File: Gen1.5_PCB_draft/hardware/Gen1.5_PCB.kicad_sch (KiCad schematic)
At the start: 35 parts, among them IC1 TJA1050T, J1 Enc1, J10 L3, J11 L4, J12 Enc2, J13 Enc3, J14 Enc4, J2 IMU, J3 Booster, J4 CAN, J5 Roboclaw1, J6 Roboclaw2, J7 Roboclaw3, J8 L1, J9 L2, U1 ESP32-P4-ETH, U2 level shifter

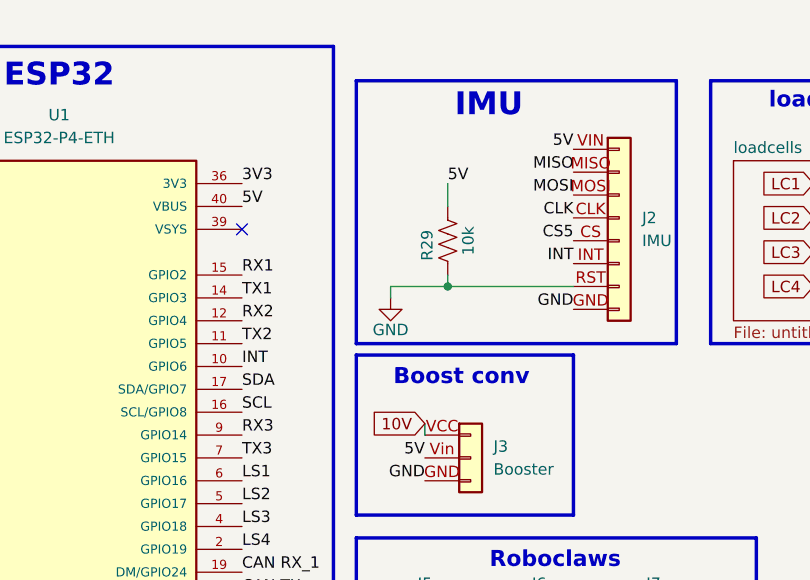
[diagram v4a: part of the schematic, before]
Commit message: fixed can test circuit via sizing
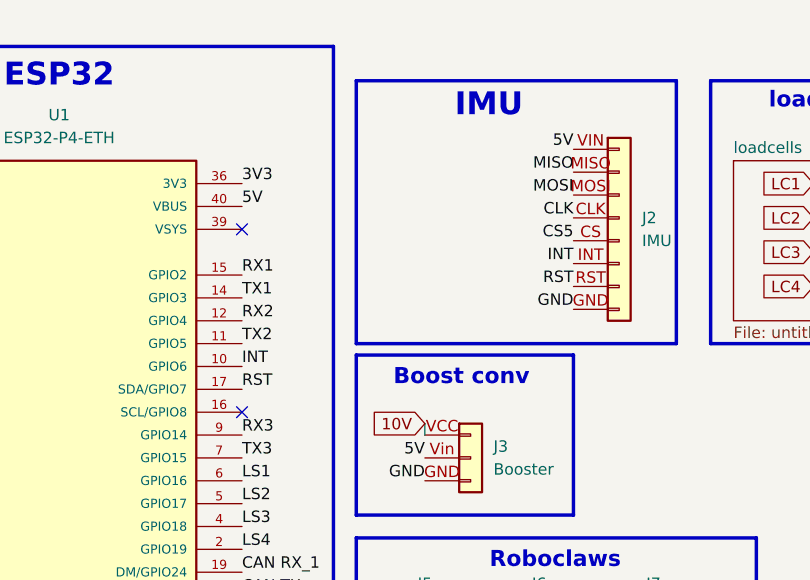
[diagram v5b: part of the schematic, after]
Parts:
- removed R29: 10k, symbol Device:R_US
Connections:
- net GND: no longer J2.RST (Pin_7)
- net SCL: no longer names the net of U1.16 (SCL/GPIO8)
- net SDA renamed RST
- net RST: now also J2.RST (Pin_7)
- no-connect marks 4 -> 5
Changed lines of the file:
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@@
 	)
 	(junction
-		(at 90.17 139.7)
-		(diameter 0)
-		(color 0 0 0 0)
-	)
-	(junction
 		(at 234.95 43.18)
 		(diameter 0)
@@
 	)
 	(no_connect
+		(at 67.31 153.67)
+	)
+	(no_connect
 		(at 26.67 138.43)
 	)
@@
 	(wire
 		(pts
-			(xy 104.14 139.7) (xy 90.17 139.7)
-		)
-		(stroke
-			(width 0)
-			(type default)
-		)
-	)
-	(wire
-		(pts
 			(xy 219.71 64.77) (xy 234.95 64.77)
 		)
@@
 	(wire
 		(pts
-			(xy 83.82 139.7) (xy 83.82 140.97)
-		)
-		(stroke
-			(width 0)
-			(type default)
-		)
-	)
-	(wire
-		(pts
 			(xy 93.98 184.15) (xy 93.98 185.42)
 		)
@@
 	(wire
 		(pts
-			(xy 90.17 139.7) (xy 83.82 139.7)
-		)
-		(stroke
-			(width 0)
-			(type default)
-		)
-	)
-	(wire
-		(pts
-			(xy 90.17 128.27) (xy 90.17 130.81)
-		)
-		(stroke
-			(width 0)
-			(type default)
-		)
-	)
-	(wire
-		(pts
 			(xy 175.26 119.38) (xy 186.69 119.38)
 		)
@@
 	(wire
 		(pts
-			(xy 90.17 138.43) (xy 90.17 139.7)
-		)
-		(stroke
-			(width 0)
-			(type default)
-		)
-	)
-	(wire
-		(pts
 			(xy 97.79 92.71) (xy 97.79 96.52)
 		)
@@
 		)
 	)
+	(label "RST"
+		(at 67.31 151.13 0)
+		(effects
+			(font
+				(size 1.27 1.27)
+			)
+			(justify left bottom)
+		)
+	)
 	(label "3V3"
 		(at 45.72 85.09 180)
@@
 		)
 	)
-	(label "SDA"
-		(at 67.31 151.13 0)
-		(effects
-			(font
-				(size 1.27 1.27)
-			)
-			(justify left bottom)
-		)
-	)
 	(label "MOSI"
 		(at 26.67 161.29 180)
@@
 		)
 	)
-	(label "5V"
-		(at 90.17 128.27 0)
-		(effects
-			(font
-				(size 1.27 1.27)
-			)
-			(justify left bottom)
-		)
-	)
 	(label "CLK"
 		(at 26.67 163.83 180)
@@
 		)
 	)
-	(label "INT"
-		(at 104.14 137.16 180)
+	(label "RST"
+		(at 104.14 139.7 180)
 		(effects
 			(font
@@
 		)
 	)
-	(label "SCL"
-		(at 67.31 153.67 0)
+	(label "INT"
+		(at 104.14 137.16 180)
 		(effects
 			(font
 				(size 1.27 1.27)
 			)
-			(justify left bottom)
+			(justify right bottom)
 		)
 	)
@@
 	(symbol
 		(lib_id "Device:R_US")
-		(at 90.17 134.62 180)
-		(unit 1)
-		(body_style 1)
-		(exclude_from_sim no)
-		(in_bom yes)
-		(on_board yes)
-		(in_pos_files yes)
-		(dnp no)
-		(property "Reference" "R29"
-			(at 87.884 135.128 90)
-			(show_name no)
-			(do_not_autoplace no)
-			(effects
-				(font
-					(size 1.27 1.27)
-				)
-			)
-		)
-		(property "Value" "10k"
-			(at 92.456 134.62 90)
-			(show_name no)
-			(do_not_autoplace no)
-			(effects
-				(font
-					(size 1.27 1.27)
-				)
-			)
-		)
-		(property "Footprint" ""
-			(at 89.154 134.366 90)
-			(hide yes)
-			(show_name no)
-			(do_not_autoplace no)
-			(effects
-				(font
-					(size 1.27 1.27)
-				)
-			)
-		)
-		(property "Datasheet" ""
-			(at 90.17 134.62 0)
-			(hide yes)
-			(show_name no)
-			(do_not_autoplace no)
-			(effects
-				(font
-					(size 1.27 1.27)
-				)
-			)
-		)
-		(property "Description" "Resistor, US symbol"
-			(at 90.17 134.62 0)
-			(hide yes)
-			(show_name no)
-			(do_not_autoplace no)
-			(effects
-				(font
-					(size 1.27 1.27)
-				)
-			)
-		)
-		(pin "1"
-		)
-		(pin "2"
-		)
-		(instances
-			(project "Gen1.5_PCB"
-				(path "/c13c24a6-83ca-4c4d-a0ab-6cb72df77012"
-					(reference "R29")
-					(unit 1)
-				)
-			)
-		)
-	)
-	(symbol
-		(lib_id "Device:R_US")
 		(at 124.46 97.79 90)
 		(unit 1)
@@
 					(unit 1)
 				)
-			)
-		)
-	)
-	(symbol
-		(lib_id "power:GND")
-		(at 83.82 140.97 0)
-		(unit 1)
-		(body_style 1)
-		(exclude_from_sim no)
-		(in_bom yes)
-		(on_board yes)
-		(in_pos_files yes)
-		(dnp no)
-		(property "Reference" "#PWR018"
-			(at 83.82 147.32 0)
-			(hide yes)
-			(show_name no)
-			(do_not_autoplace no)
-			(effects
-				(font
-					(size 1.27 1.27)
-				)
-			)
-		)
-		(property "Value" "GND"
-			(at 83.82 144.526 0)
-			(show_name no)
-			(do_not_autoplace no)
-			(effects
-				(font
-					(size 1.27 1.27)
-				)
-			)
-		)
-		(property "Footprint" ""
-			(at 83.82 140.97 0)
-			(hide yes)
-			(show_name no)
-			(do_not_autoplace no)
-			(effects
-				(font
-					(size 1.27 1.27)
-				)
-			)
-		)
-		(property "Datasheet" ""
-			(at 83.82 140.97 0)
-			(hide yes)
-			(show_name no)
-			(do_not_autoplace no)
-			(effects
-				(font
-					(size 1.27 1.27)
-				)
-			)
-		)
-		(property "Description" "Power symbol creates a global label with name \"GND\" , ground"
-			(at 83.82 140.97 0)
-			(hide yes)
-			(show_name no)
-			(do_not_autoplace no)
-			(effects
-				(font
-					(size 1.27 1.27)
-				)
-			)
-		)
-		(pin "1"
-		)
-		(instances
-			(project "Gen1.5_PCB"
-				(path "/c13c24a6-83ca-4c4d-a0ab-6cb72df77012"
-					(reference "#PWR018")
-					(unit 1)
-				)

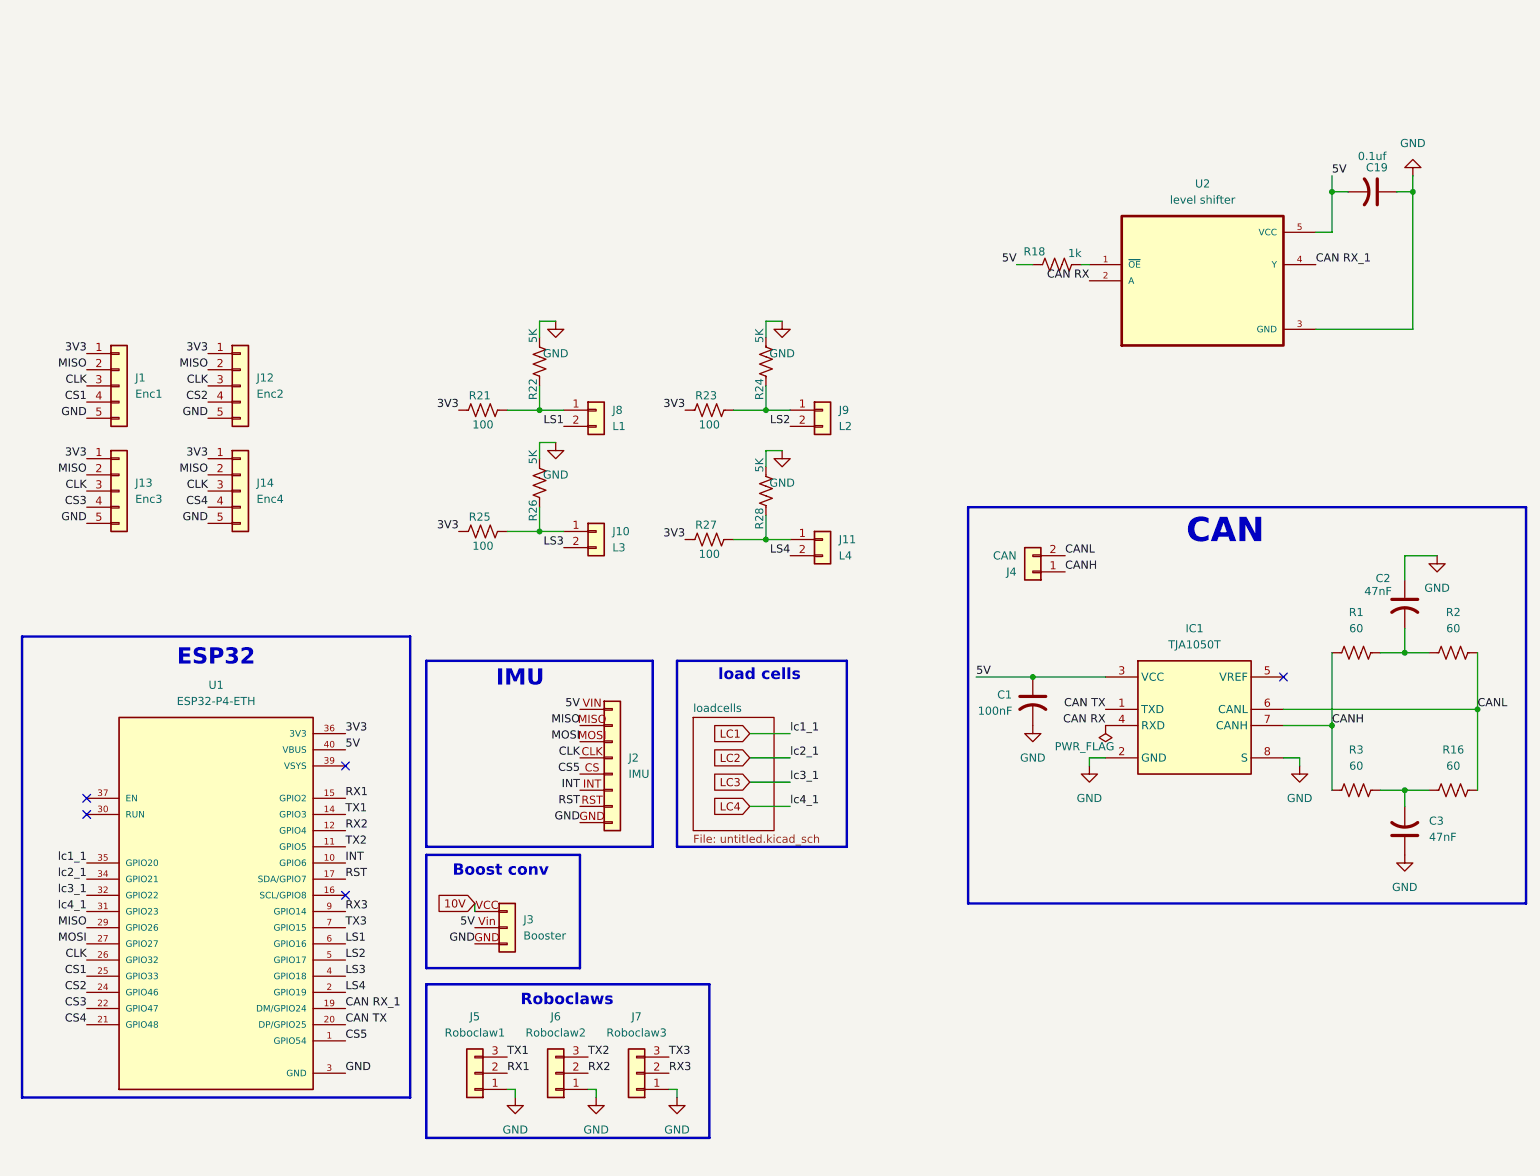
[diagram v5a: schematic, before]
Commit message: fixed can circuit on gen1.5 draft and added jumpers between roboclaw uart and can
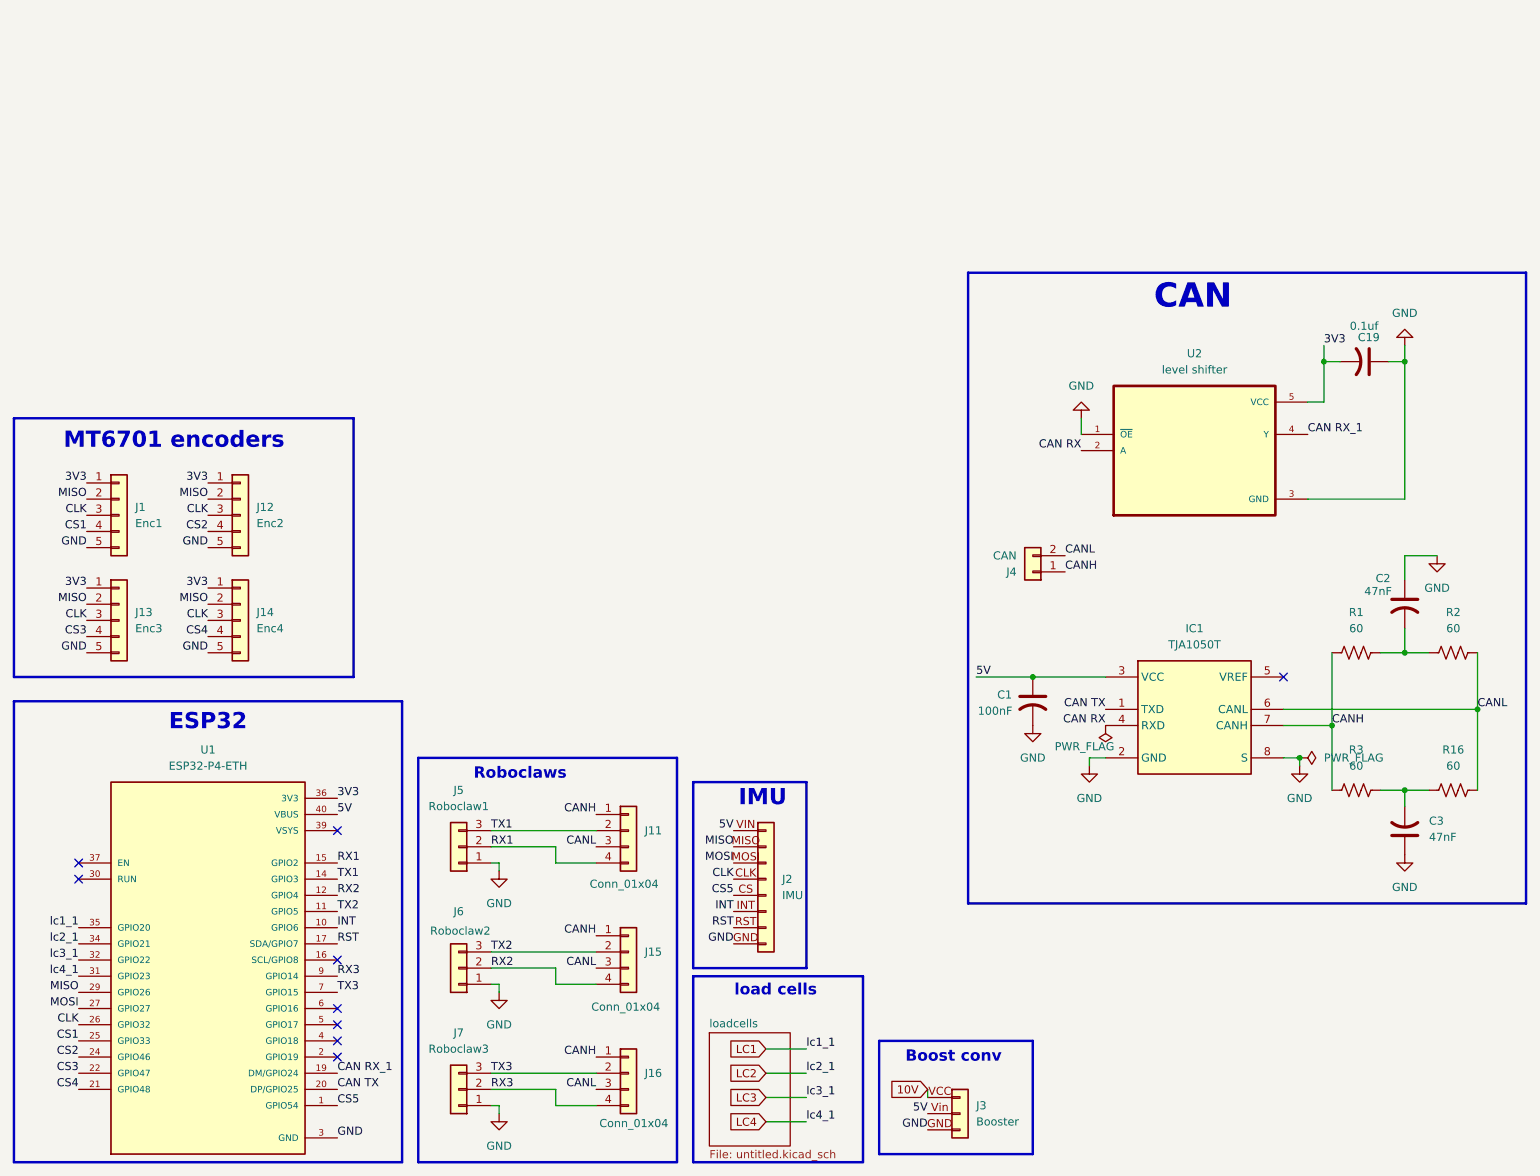
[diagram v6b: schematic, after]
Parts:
- removed J10: L3, symbol Connector_Generic:Conn_01x02
- removed J11: L4, symbol Connector_Generic:Conn_01x02
- removed J8: L1, symbol Connector_Generic:Conn_01x02
- removed J9: L2, symbol Connector_Generic:Conn_01x02
- removed R18: 1k, symbol Device:R_US
- removed R21, R23, R25, R27: 100, symbol Device:R_US
- removed R22, R24, R26, R28: 5K, symbol Device:R_US
- added J11, J15, J16: Conn_01x04, symbol Connector_Generic:Conn_01x04
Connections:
- net 3V3: now also C19.2, U2.5 (VCC)
- net 5V: no longer C19.2, U2.5 (VCC)
- net CANH: now also J11.1 (Pin_1), J15.1 (Pin_1), J16.1 (Pin_1)
- net CANL: now also J11.3 (Pin_3), J15.3 (Pin_3), J16.3 (Pin_3)
- net GND: now also U2.1 (~{OE})
- net RX1: now also J11.4 (Pin_4)
- net RX2: now also J15.4 (Pin_4)
- net RX3: now also J16.4 (Pin_4)
- net TX1: now also J11.2 (Pin_2)
- net TX2: now also J15.2 (Pin_2)
- net TX3: now also J16.2 (Pin_2)
- net LS1: no longer names the net of U1.6 (GPIO16)
- net LS2: no longer names the net of U1.5 (GPIO17)
- net LS3: no longer names the net of U1.4 (GPIO18)
- net LS4: no longer names the net of U1.2 (GPIO19)
- no-connect marks 5 -> 9
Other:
- note added: "MT6701 encoders"
- moved on the sheet: C19, J1, J12, J13, J14, J2, J3, J5, J6, J7, U1, U2

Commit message: removed can circuit
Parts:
- removed C1: 100nF, symbol Device:C_US
- removed C19: 0.1uf, symbol Device:C_US
- removed C2, C3: 47nF, symbol Device:C_US
- removed IC1: TJA1050T, Gen1.5_PCB:TJA1050T, symbol Gen1.5_PCB:TJA1050T
- removed J11, J15, J16: Conn_01x04, symbol Connector_Generic:Conn_01x04
- removed J4: CAN, symbol Connector_Generic:Conn_01x02
- removed R1, R16, R2, R3: 60, symbol Device:R_US
- removed U2: level shifter, SN74LVC1G125DBVR:SOT95P280X145-5N, symbol Gen1.5_PCB:SN74LVC1G125DBVR
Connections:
- net CAN RX_1: no longer names the net of U1.19 (DM/GPIO24)
- net CAN TX: no longer names the net of U1.20 (DP/GPIO25)
- no-connect marks 9 -> 10
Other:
- note removed: "CAN"
- moved on the sheet: J2, J3
